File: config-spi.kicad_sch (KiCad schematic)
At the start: 34 parts, among them J3001 PinHeader_2x7_P2mm_SMD_Shroud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, Q3001 BSS138PW, Q3002 BSS138PW, U3001 S25FL128SAGNFI000, U3002 XC7K160T-FFG676

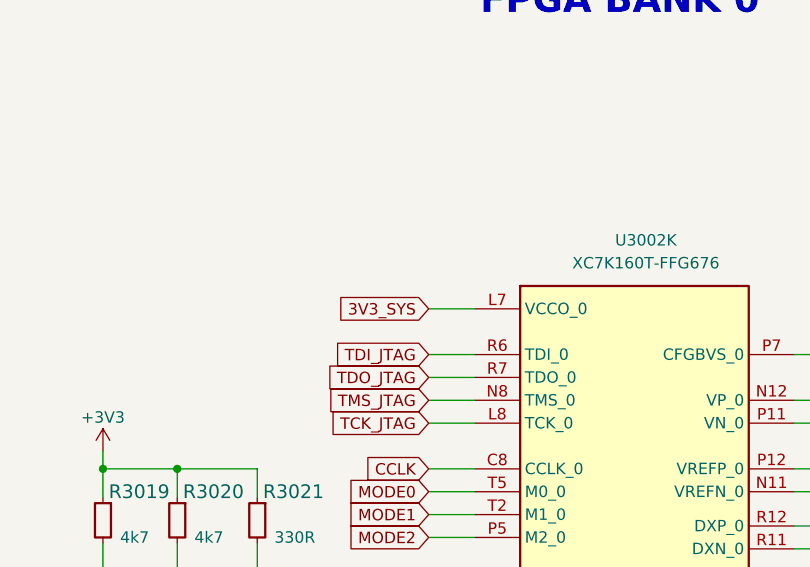
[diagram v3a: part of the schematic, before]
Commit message: Create FPGA decoupling, start creating power planes
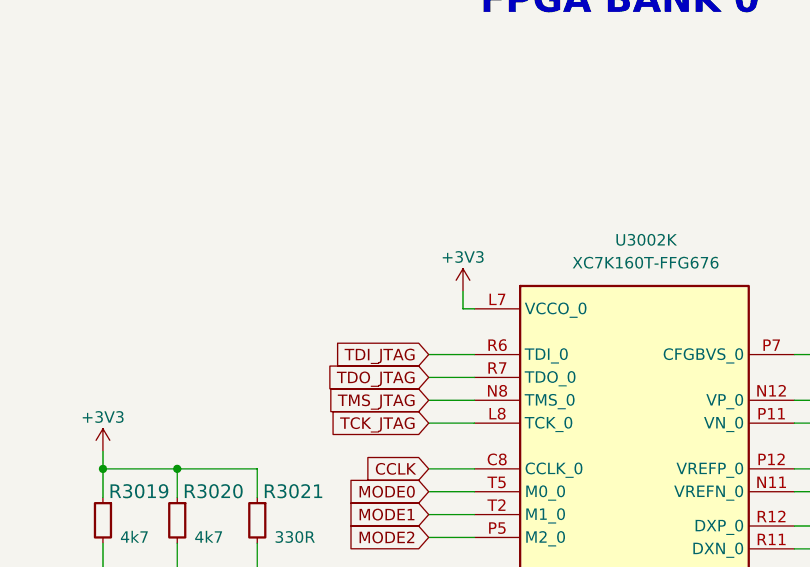
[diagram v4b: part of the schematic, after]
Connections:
- net 3V3_SYS is gone; now on net +3V3: U3002.L7 (VCCO_0), U3002.T6 (VCCO_0)
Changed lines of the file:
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@@
     (stroke (width 0) (type default) (color 0 0 0 0))
   )
+  (wire (pts (xy 284.48 87.63) (xy 285.75 87.63))
+    (stroke (width 0) (type default) (color 0 0 0 0))
+  )
   (wire (pts (xy 244.475 120.65) (xy 285.75 120.65))
     (stroke (width 0) (type default) (color 0 0 0 0))
@@
     (stroke (width 0) (type default) (color 0 0 0 0))
   )
+  (wire (pts (xy 284.48 85.725) (xy 284.48 87.63))
+    (stroke (width 0) (type default) (color 0 0 0 0))
+  )
   (wire (pts (xy 244.475 105.41) (xy 252.73 105.41))
     (stroke (width 0) (type default) (color 0 0 0 0))
@@
     (stroke (width 0) (type default) (color 0 0 0 0))
   )
-  (wire (pts (xy 280.67 87.63) (xy 285.75 87.63))
-    (stroke (width 0) (type default) (color 0 0 0 0))
-  )
   (wire (pts (xy 36.83 232.41) (xy 36.83 234.95))
     (stroke (width 0) (type default) (color 0 0 0 0))
@@
     )
   )
-  (global_label "3V3_SYS" (shape input) (at 280.67 87.63 180) (fields_autoplaced)
-    (effects (font (size 1.27 1.27)) (justify right))
-    (property "Intersheet References" "${INTERSHEET_REFS}" (id 0) (at 212.09 392.43 0)
-      (effects (font (size 1.27 1.27)) hide)
-    )
-  )
   (global_label "MODE2" (shape input) (at 222.885 262.89 180) (fields_autoplaced)
     (effects (font (size 1.27 1.27)) (justify right))
@@
     (pin "1")
   )
+  (symbol (lib_id "power:+3V3") (at 284.48 85.725 0) (unit 1)
+    (in_bom yes) (on_board yes)
+    (property "Reference" "#PWR0179" (id 0) (at 284.48 89.535 0)
+      (effects (font (size 1.27 1.27)) hide)
+    )
+    (property "Value" "+3V3" (id 1) (at 284.48 81.915 0))
+    (property "Footprint" "" (id 2) (at 284.48 85.725 0)
+      (effects (font (size 1.27 1.27)) hide)
+    )
+    (property "Datasheet" "" (id 3) (at 284.48 85.725 0)
+      (effects (font (size 1.27 1.27)) hide)
+    )
+    (pin "1")
+  )
   (symbol (lib_id "power:+3V3") (at 141.605 238.125 90) (unit 1)
     (in_bom yes) (on_board yes)
-    (property "Reference" "#PWR?" (id 0) (at 145.415 238.125 0)
+    (property "Reference" "#PWR0123" (id 0) (at 145.415 238.125 0)
       (effects (font (size 1.27 1.27)) hide)
     )
@@
   (symbol (lib_id "power:+3V3") (at 222.885 252.095 90) (unit 1)
     (in_bom yes) (on_board yes)
-    (property "Reference" "#PWR?" (id 0) (at 226.695 252.095 0)
+    (property "Reference" "#PWR0116" (id 0) (at 226.695 252.095 0)
       (effects (font (size 1.27 1.27)) hide)
     )
@@
   (symbol (lib_id "power:+3V3") (at 111.125 86.995 0) (unit 1)
     (in_bom yes) (on_board yes)
-    (property "Reference" "#PWR?" (id 0) (at 111.125 90.805 0)
+    (property "Reference" "#PWR0122" (id 0) (at 111.125 90.805 0)
       (effects (font (size 1.27 1.27)) hide)
     )
@@
   (symbol (lib_id "power:+3V3") (at 240.665 243.205 270) (unit 1)
     (in_bom yes) (on_board yes)
-    (property "Reference" "#PWR?" (id 0) (at 236.855 243.205 0)
+    (property "Reference" "#PWR0117" (id 0) (at 236.855 243.205 0)
       (effects (font (size 1.27 1.27)) hide)
     )
@@
   (symbol (lib_id "power:+3V3") (at 55.245 222.885 0) (unit 1)
     (in_bom yes) (on_board yes)
-    (property "Reference" "#PWR?" (id 0) (at 55.245 226.695 0)
+    (property "Reference" "#PWR0125" (id 0) (at 55.245 226.695 0)
       (effects (font (size 1.27 1.27)) hide)
     )
@@
   (symbol (lib_id "power:+3V3") (at 329.184 217.17 0) (unit 1)
     (in_bom yes) (on_board yes)
-    (property "Reference" "#PWR?" (id 0) (at 329.184 220.98 0)
+    (property "Reference" "#PWR0113" (id 0) (at 329.184 220.98 0)
       (effects (font (size 1.27 1.27)) hide)
     )
@@
   (symbol (lib_id "power:+3V3") (at 73.025 100.965 0) (unit 1)
     (in_bom yes) (on_board yes)
-    (property "Reference" "#PWR?" (id 0) (at 73.025 104.775 0)
+    (property "Reference" "#PWR0120" (id 0) (at 73.025 104.775 0)
       (effects (font (size 1.27 1.27)) hide)
     )
@@
   (symbol (lib_id "power:+3V3") (at 240.665 230.505 270) (unit 1)
     (in_bom yes) (on_board yes)
-    (property "Reference" "#PWR?" (id 0) (at 236.855 230.505 0)
+    (property "Reference" "#PWR0115" (id 0) (at 236.855 230.505 0)
       (effects (font (size 1.27 1.27)) hide)
     )
@@
   (symbol (lib_id "power:+3V3") (at 244.475 103.505 0) (unit 1)
     (in_bom yes) (on_board yes)
-    (property "Reference" "#PWR?" (id 0) (at 244.475 107.315 0)
+    (property "Reference" "#PWR0119" (id 0) (at 244.475 107.315 0)
       (effects (font (size 1.27 1.27)) hide)
     )
@@
   (symbol (lib_id "power:+3V3") (at 48.895 102.87 0) (unit 1)
     (in_bom yes) (on_board yes)
-    (property "Reference" "#PWR?" (id 0) (at 48.895 106.68 0)
+    (property "Reference" "#PWR0121" (id 0) (at 48.895 106.68 0)
       (effects (font (size 1.27 1.27)) hide)
     )
@@
   (symbol (lib_id "power:+3V3") (at 363.22 90.805 0) (unit 1)
     (in_bom yes) (on_board yes)
-    (property "Reference" "#PWR?" (id 0) (at 363.22 94.615 0)
+    (property "Reference" "#PWR0114" (id 0) (at 363.22 94.615 0)
       (effects (font (size 1.27 1.27)) hide)
     )
@@
   (symbol (lib_id "power:+3V3") (at 327.66 78.74 0) (unit 1)
     (in_bom yes) (on_board yes)
-    (property "Reference" "#PWR?" (id 0) (at 327.66 82.55 0)
+    (property "Reference" "#PWR0118" (id 0) (at 327.66 82.55 0)
       (effects (font (size 1.27 1.27)) hide)
     )
@@
   (symbol (lib_id "power:+3V3") (at 141.605 257.81 90) (unit 1)
     (in_bom yes) (on_board yes)
-    (property "Reference" "#PWR?" (id 0) (at 145.415 257.81 0)
+    (property "Reference" "#PWR0124" (id 0) (at 145.415 257.81 0)
       (effects (font (size 1.27 1.27)) hide)
     )

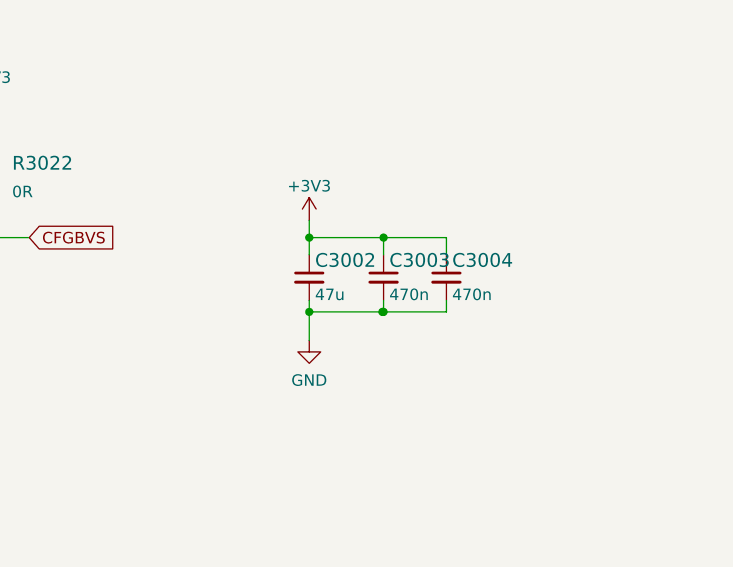
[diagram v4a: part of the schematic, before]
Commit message: Improve DDR assigment, connect ECC to remaining pins, cleanup not used components, continue placement of misc. components
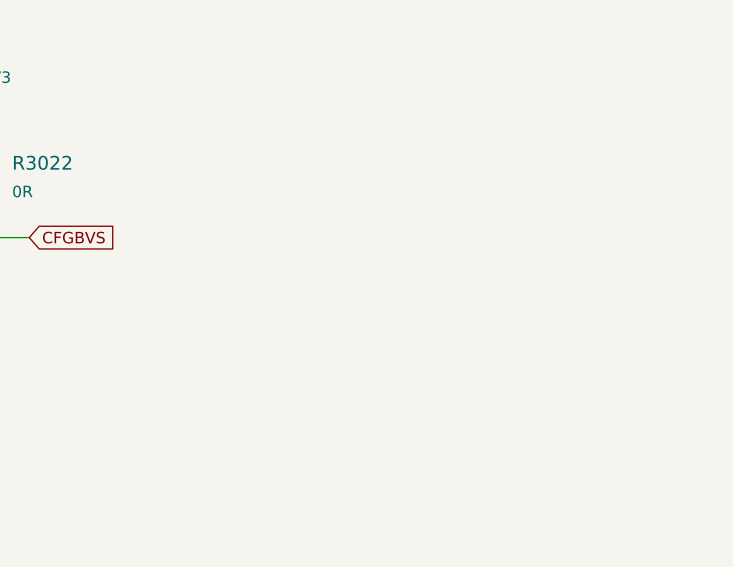
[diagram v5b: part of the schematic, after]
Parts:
- removed C3002: C_47u_0603, data-center-rdimm-ddr4-tester-footprints:C_0603_1608Metric, symbol data-center-rdimm-ddr4-tester:C_47u_0603
- removed C3003, C3004: C_470n_0402, data-center-rdimm-ddr4-tester-footprints:C_0402_1005Metric, symbol data-center-rdimm-ddr4-tester:C_470n_0402
- R3022: footprint data-center-rdimm-ddr4-tester-footprints:R_0402_1005Metric -> antmicro-footprints:R_0402_1005Metric_EIA

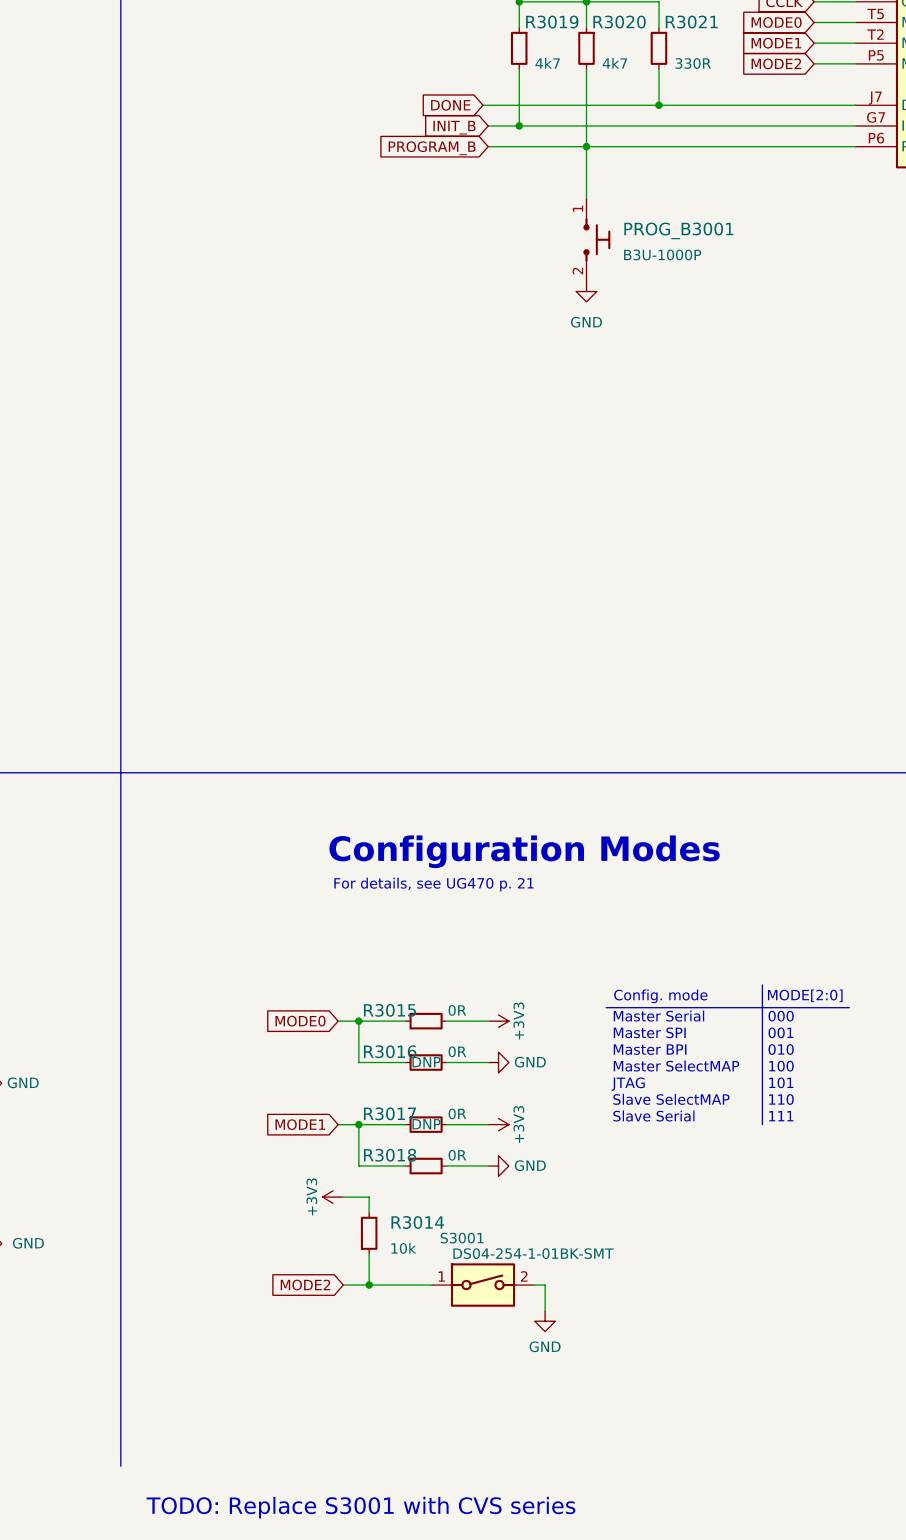
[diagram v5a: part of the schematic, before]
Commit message: Schematic cleanup, connect VINT DC-DC, continue placing misc. circuits
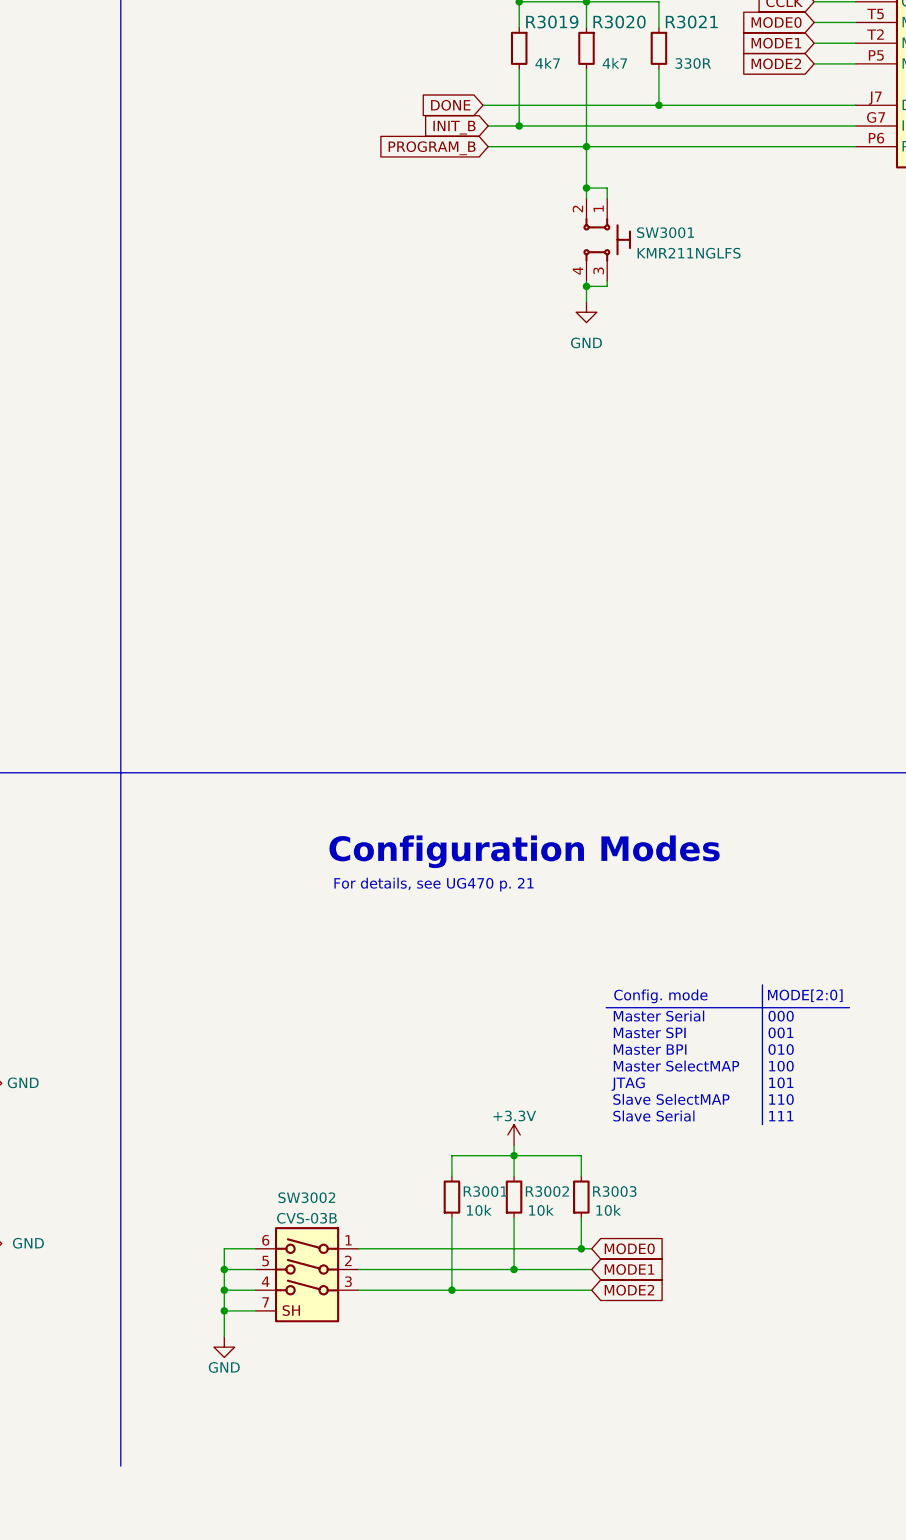
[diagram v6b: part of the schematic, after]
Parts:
- removed PROG_B3001: SW_B3U-1000P, data-center-rdimm-ddr4-tester-footprints:SW_B3U-3000P, symbol data-center-rdimm-ddr4-tester:SW_B3U-1000P
- removed R3014: R_10k_0402, data-center-rdimm-ddr4-tester-footprints:R_0402_1005Metric, symbol data-center-rdimm-ddr4-tester:R_10k_0402
- removed R3015, R3016, R3017, R3018: R_0R_0402, data-center-rdimm-ddr4-tester-footprints:R_0402_1005Metric, symbol data-center-rdimm-ddr4-tester:R_0R_0402
- removed S3001: SW_DS04-254-1-01BK-SMT, data-center-rdimm-ddr4-tester-footprints:SW_DS04-254-1-01BK-SMT, symbol data-center-rdimm-ddr4-tester:SW_DS04-254-1-01BK-SMT
- added R3001, R3002, R3003: R_10k_0402, antmicro-footprints:R_0402_1005Metric, symbol antmicroResistors0402:R_10k_0402
- added SW3001: SW_KMR211NGLFS_SMD, antmicro-footprints:SW_KMR211NGLFS_SMD, symbol antmicroPushbuttonSwitches:SW_KMR211NGLFS_SMD
- added SW3002: CVS-03B, antmicro-footprints:SW_DIP_SPSTx03_Slide_Copal_CVS-03xB_W5.9mm_P1mm, symbol antmicroSlideSwitches:CVS-03B
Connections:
- net +3V3: now also R3001.2, R3002.2, R3003.2
- net GND: now also SW3001.3, SW3001.4, SW3002.4, SW3002.5, SW3002.6, SW3002.7
- net MODE0: now also R3003.1, SW3002.1
- net MODE1: now also R3002.1, SW3002.2
- net MODE2: now also R3001.1, SW3002.3
- net PROGRAM_B: now also SW3001.1, SW3001.2
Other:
- note removed: "TODO: Replace S3001 with CVS series"

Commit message: Add loclib
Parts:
- C3001: footprint data-center-rdimm-ddr4-tester-footprints:C_0402_1005Metric -> sodimm-ddr5-tester-footprints:C_0402_1005Metric; symbol data-center-rdimm-ddr4-tester:C_100n_0402 -> sodimm-ddr5-tester:C_100n_0402
- D3001: footprint data-center-rdimm-ddr4-tester-footprints:USON-14_3.5X1.3X0.5mm_P0.5mm -> sodimm-ddr5-tester-footprints:USON-14_3.5X1.3X0.5mm_P0.5mm; symbol data-center-rdimm-ddr4-tester:TPD6E05U06RVZR -> sodimm-ddr5-tester:TPD6E05U06RVZR
- D3002, D3003: footprint data-center-rdimm-ddr4-tester-footprints:LED_0603_1608Metric_G -> sodimm-ddr5-tester-footprints:LED_0603_1608Metric_G; symbol data-center-rdimm-ddr4-tester:LED_G_0603_KP-1608CGCK -> sodimm-ddr5-tester:LED_G_0603_KP-1608CGCK
- EMCCLK3001, PUDC_B3001: footprint data-center-rdimm-ddr4-tester-footprints:Testpoint_smd_1mm -> sodimm-ddr5-tester-footprints:Testpoint_smd_1mm; symbol data-center-rdimm-ddr4-tester:TP_1mm_SMD -> sodimm-ddr5-tester:TP_1mm_SMD
- J3001: footprint data-center-rdimm-ddr4-tester-footprints:PinHeader_2x7_P2mm_SMD_Shrouded_no-locator -> sodimm-ddr5-tester-footprints:PinHeader_2x7_P2mm_SMD_Shrouded_no-locator; symbol data-center-rdimm-ddr4-tester:PinHeader_2x7_P2mm_SMD_Shrouded_no-locator -> sodimm-ddr5-tester:PinHeader_2x7_P2mm_SMD_Shrouded_no-locator
- Q3001, Q3002: footprint data-center-rdimm-ddr4-tester-footprints:SC70-3 -> sodimm-ddr5-tester-footprints:SC70-3; symbol data-center-rdimm-ddr4-tester:BSS138PW -> sodimm-ddr5-tester:BSS138PW
- R3001, R3002, R3003: footprint antmicro-footprints:R_0402_1005Metric -> sodimm-ddr5-tester-footprints:R_0402_1005Metric; symbol antmicroResistors0402:R_10k_0402 -> sodimm-ddr5-tester:R_10k_0402
- R3007: footprint data-center-rdimm-ddr4-tester-footprints:R_0402_1005Metric -> sodimm-ddr5-tester-footprints:R_0402_1005Metric; symbol data-center-rdimm-ddr4-tester:R_2k2_0402 -> sodimm-ddr5-tester:R_2k2_0402
- R3008, R3009, R3023, R3024: footprint data-center-rdimm-ddr4-tester-footprints:R_0402_1005Metric -> sodimm-ddr5-tester-footprints:R_0402_1005Metric; symbol data-center-rdimm-ddr4-tester:R_100R_0402 -> sodimm-ddr5-tester:R_100R_0402
- R3010, R3011, R3019, R3020: footprint data-center-rdimm-ddr4-tester-footprints:R_0402_1005Metric -> sodimm-ddr5-tester-footprints:R_0402_1005Metric; symbol data-center-rdimm-ddr4-tester:R_4k7_0402 -> sodimm-ddr5-tester:R_4k7_0402
- R3012, R3013, R3021: footprint data-center-rdimm-ddr4-tester-footprints:R_0402_1005Metric -> sodimm-ddr5-tester-footprints:R_0402_1005Metric; symbol data-center-rdimm-ddr4-tester:R_330R_0402 -> sodimm-ddr5-tester:R_330R_0402
- R3022: footprint antmicro-footprints:R_0402_1005Metric_EIA -> sodimm-ddr5-tester-footprints:R_0402_1005Metric_EIA; symbol data-center-rdimm-ddr4-tester:R_0R_0402 -> sodimm-ddr5-tester:R_0R_0402
- SW3001: footprint antmicro-footprints:SW_KMR211NGLFS_SMD -> sodimm-ddr5-tester-footprints:SW_KMR211NGLFS_SMD; symbol antmicroPushbuttonSwitches:SW_KMR211NGLFS_SMD -> sodimm-ddr5-tester:SW_KMR211NGLFS_SMD
- SW3002: footprint antmicro-footprints:SW_DIP_SPSTx03_Slide_Copal_CVS-03xB_W5.9mm_P1mm -> sodimm-ddr5-tester-footprints:SW_DIP_SPSTx03_Slide_Copal_CVS-03xB_W5.9mm_P1mm; symbol antmicroSlideSwitches:CVS-03B -> sodimm-ddr5-tester:CVS-03B
- U3001: footprint data-center-rdimm-ddr4-tester-footprints:WSON-8_6x8x0.5mm_P1.27mm -> sodimm-ddr5-tester-footprints:WSON-8_6x8x0.5mm_P1.27mm; symbol data-center-rdimm-ddr4-tester:S25FL128SAGNFI000 -> sodimm-ddr5-tester:S25FL128SAGNFI000
- U3002: footprint data-center-rdimm-ddr4-tester-footprints:BGA-676_27x27mm_Layout26x26_P1X1mm -> sodimm-ddr5-tester-footprints:BGA-676_27x27mm_Layout26x26_P1X1mm; symbol data-center-rdimm-ddr4-tester:XC7K160T-FFG676 -> sodimm-ddr5-tester:XC7K160T-FFG676
